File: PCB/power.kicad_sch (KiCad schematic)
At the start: 7 parts, among them U4 TPS628438DRL, U5 TPS3839K33

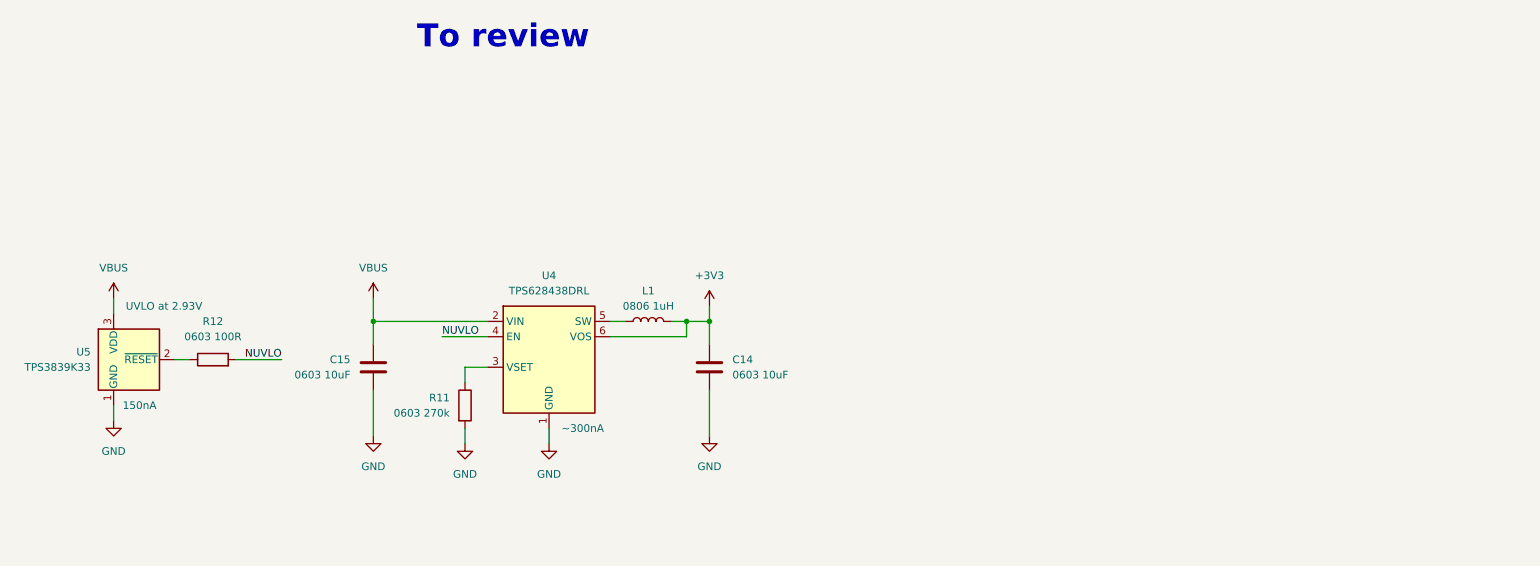
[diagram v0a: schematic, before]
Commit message: added power block, pheripherial
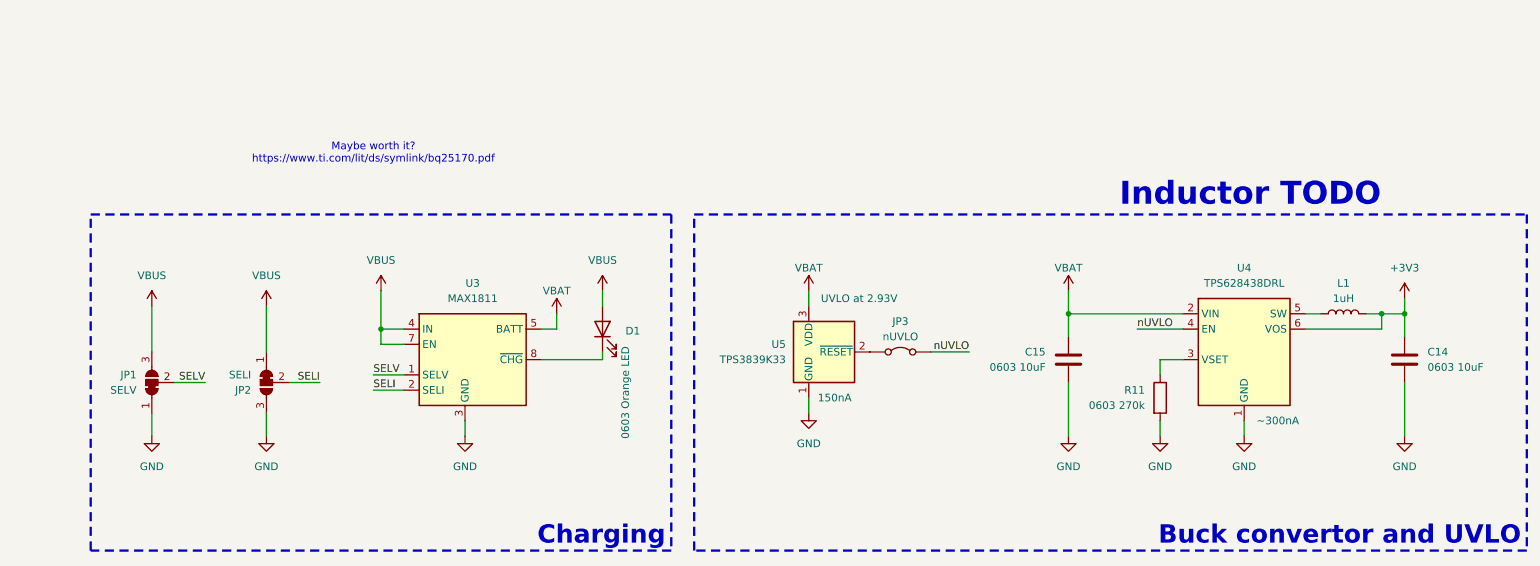
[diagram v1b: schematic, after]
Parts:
- removed R12: 0603 100R, symbol Device:R
- added D1: 0603 Orange LED, LED_SMD:LED_0603_1608Metric_Pad1.05x0.95mm_HandSolder, symbol Device:LED
- added JP1: SELV, symbol Jumper:SolderJumper_3_Bridged12
- added JP2: SELI, symbol Jumper:SolderJumper_3_Bridged12
- added JP3: nUVLO, symbol Jumper:Jumper_2_Bridged
- added U3: MAX1811, Package_SO:SOIC-8_3.9x4.9mm_P1.27mm, symbol Battery_Management:MAX1811
- L1: value 0806 1uH -> 1uH
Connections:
- net GND: now also JP1.1 (A), JP2.3 (B), U3.3 (GND), U3.6 (GND)
- net VBUS: now also D1.2 (A), JP1.3 (B), JP2.1 (A), U3.4 (IN), U3.7 (EN); no longer C15.1, U4.2 (VIN), U5.3 (VDD)
- net at U5.2 (~{RESET}): now also JP3.1 (A)
- net NUVLO renamed nUVLO
- net nUVLO: now also JP3.2 (B)
- new net: D1.1 (K), U3.8 (~{CHG})
- new net SELI: JP2.2 (C), U3.2 (SELI)
- new net SELV: JP1.2 (C), U3.1 (SELV)
- new net VBAT: C15.1, U3.5 (BATT), U4.2 (VIN), U5.3 (VDD)
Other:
- note added: "Inductor TODO"
- note added: "Maybe worth it? https://www.ti.com/lit/ds/symlink/bq25170.pdf"
- note removed: "To review"
- moved on the sheet: C14, C15, L1, R11, U4, U5

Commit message: added GPS, charging IC, SHT41, and started working on the RF
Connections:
- net GND renamed GNDREF
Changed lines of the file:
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@@
 	)
 	(symbol
-		(lib_id "power:GND")
+		(lib_id "power:GNDREF")
 		(at 190.5 113.03 0)
 		(unit 1)
@@
 		(dnp no)
 		(fields_autoplaced yes)
-		(property "Reference" "#PWR040"
+		(property "Reference" "#PWR40"
 			(at 190.5 119.38 0)
 			(hide yes)
@@
 			)
 		)
-		(property "Value" "GND"
+		(property "Value" "GNDREF"
 			(at 190.5 118.11 0)
 			(show_name no)
@@
 			)
 		)
-		(property "Description" "Power symbol creates a global label with name \"GND\" , ground"
+		(property "Description" "Power symbol creates a global label with name \"GNDREF\" , reference supply ground"
 			(at 190.5 113.03 0)
 			(hide yes)
@@
 			(project "PawBuddy_PCB"
 				(path "/ddc031a5-f801-471f-9629-7d18bb02ea71/bbb75299-8683-40e9-bcaa-d3bebe81f345"
-					(reference "#PWR040")
-					(unit 1)
-				)
-			)
-		)
-	)
-	(symbol
-		(lib_id "power:GND")
+					(reference "#PWR40")
+					(unit 1)
+				)
+			)
+		)
+	)
+	(symbol
+		(lib_id "power:GNDREF")
 		(at 246.38 113.03 0)
 		(unit 1)
@@
 		(dnp no)
 		(fields_autoplaced yes)
-		(property "Reference" "#PWR041"
+		(property "Reference" "#PWR41"
 			(at 246.38 119.38 0)
 			(hide yes)
@@
 			)
 		)
-		(property "Value" "GND"
+		(property "Value" "GNDREF"
 			(at 246.38 118.11 0)
 			(show_name no)
@@
 			)
 		)
-		(property "Description" "Power symbol creates a global label with name \"GND\" , ground"
+		(property "Description" "Power symbol creates a global label with name \"GNDREF\" , reference supply ground"
 			(at 246.38 113.03 0)
 			(hide yes)
@@
 			(project "PawBuddy_PCB"
 				(path "/ddc031a5-f801-471f-9629-7d18bb02ea71/bbb75299-8683-40e9-bcaa-d3bebe81f345"
-					(reference "#PWR041")
+					(reference "#PWR41")
 					(unit 1)
 				)
@@
 	)
 	(symbol
-		(lib_id "power:GND")
+		(lib_id "power:GNDREF")
 		(at 57.15 113.03 0)
 		(unit 1)
@@
 		(dnp no)
 		(fields_autoplaced yes)
-		(property "Reference" "#PWR049"
+		(property "Reference" "#PWR49"
 			(at 57.15 119.38 0)
 			(hide yes)
@@
 			)
 		)
-		(property "Value" "GND"
+		(property "Value" "GNDREF"
 			(at 57.15 118.11 0)
 			(show_name no)
@@
 			)
 		)
-		(property "Description" "Power symbol creates a global label with name \"GND\" , ground"
+		(property "Description" "Power symbol creates a global label with name \"GNDREF\" , reference supply ground"
 			(at 57.15 113.03 0)
 			(hide yes)
@@
 			(project "PawBuddy_PCB"
 				(path "/ddc031a5-f801-471f-9629-7d18bb02ea71/bbb75299-8683-40e9-bcaa-d3bebe81f345"
-					(reference "#PWR049")
-					(unit 1)
-				)
-			)
-		)
-	)
-	(symbol
-		(lib_id "power:GND")
+					(reference "#PWR49")
+					(unit 1)
+				)
+			)
+		)
+	)
+	(symbol
+		(lib_id "power:GNDREF")
 		(at 147.32 109.22 0)
 		(unit 1)
@@
 		(dnp no)
 		(fields_autoplaced yes)
-		(property "Reference" "#PWR038"
+		(property "Reference" "#PWR38"
 			(at 147.32 115.57 0)
 			(hide yes)
@@
 			)
 		)
-		(property "Value" "GND"
+		(property "Value" "GNDREF"
 			(at 147.32 114.3 0)
 			(show_name no)
@@
 			)
 		)
-		(property "Description" "Power symbol creates a global label with name \"GND\" , ground"
+		(property "Description" "Power symbol creates a global label with name \"GNDREF\" , reference supply ground"
 			(at 147.32 109.22 0)
 			(hide yes)
@@
 			(project "PawBuddy_PCB"
 				(path "/ddc031a5-f801-471f-9629-7d18bb02ea71/bbb75299-8683-40e9-bcaa-d3bebe81f345"
-					(reference "#PWR038")
+					(reference "#PWR38")
 					(unit 1)
 				)
@@
 	)
 	(symbol
-		(lib_id "power:GND")
+		(lib_id "power:GNDREF")
 		(at 90.17 113.03 0)
 		(unit 1)
@@
 		(dnp no)
 		(fields_autoplaced yes)
-		(property "Reference" "#PWR046"
+		(property "Reference" "#PWR46"
 			(at 90.17 119.38 0)
 			(hide yes)
@@
 			)
 		)
-		(property "Value" "GND"
+		(property "Value" "GNDREF"
 			(at 90.17 118.11 0)
 			(show_name no)
@@
 			)
 		)
-		(property "Description" "Power symbol creates a global label with name \"GND\" , ground"
+		(property "Description" "Power symbol creates a global label with name \"GNDREF\" , reference supply ground"
 			(at 90.17 113.03 0)
 			(hide yes)
@@
 			(project "PawBuddy_PCB"
 				(path "/ddc031a5-f801-471f-9629-7d18bb02ea71/bbb75299-8683-40e9-bcaa-d3bebe81f345"
-					(reference "#PWR046")
+					(reference "#PWR46")
 					(unit 1)
 				)
@@
 	)
 	(symbol
-		(lib_id "power:GND")
+		(lib_id "power:GNDREF")
 		(at 38.1 113.03 0)
 		(unit 1)
@@
 		(dnp no)
 		(fields_autoplaced yes)
-		(property "Reference" "#PWR045"
+		(property "Reference" "#PWR45"
 			(at 38.1 119.38 0)
 			(hide yes)
@@
 			)
 		)
-		(property "Value" "GND"
+		(property "Value" "GNDREF"
 			(at 38.1 118.11 0)
 			(show_name no)
@@
 			)
 		)
-		(property "Description" "Power symbol creates a global label with name \"GND\" , ground"
+		(property "Description" "Power symbol creates a global label with name \"GNDREF\" , reference supply ground"
 			(at 38.1 113.03 0)
 			(hide yes)
@@
 			(project "PawBuddy_PCB"
 				(path "/ddc031a5-f801-471f-9629-7d18bb02ea71/bbb75299-8683-40e9-bcaa-d3bebe81f345"
-					(reference "#PWR045")
-					(unit 1)
-				)
-			)
-		)
-	)
-	(symbol
-		(lib_id "power:GND")
+					(reference "#PWR45")
+					(unit 1)
+				)
+			)
+		)
+	)
+	(symbol
+		(lib_id "power:GNDREF")
 		(at 219.71 113.03 0)
 		(unit 1)
@@
 		(dnp no)
 		(fields_autoplaced yes)
-		(property "Reference" "#PWR037"
+		(property "Reference" "#PWR37"
 			(at 219.71 119.38 0)
 			(hide yes)
@@
 			)
 		)
-		(property "Value" "GND"
+		(property "Value" "GNDREF"
 			(at 219.71 118.11 0)
 			(show_name no)
@@
 			)
 		)
-		(property "Description" "Power symbol creates a global label with name \"GND\" , ground"
+		(property "Description" "Power symbol creates a global label with name \"GNDREF\" , reference supply ground"
 			(at 219.71 113.03 0)
 			(hide yes)
@@
 			(project "PawBuddy_PCB"
 				(path "/ddc031a5-f801-471f-9629-7d18bb02ea71/bbb75299-8683-40e9-bcaa-d3bebe81f345"
-					(reference "#PWR037")
+					(reference "#PWR37")
 					(unit 1)
 				)
@@
 	)
 	(symbol
-		(lib_id "power:GND")
+		(lib_id "power:GNDREF")
 		(at 205.74 113.03 0)
 		(unit 1)
@@
 		(dnp no)
 		(fields_autoplaced yes)
-		(property "Reference" "#PWR039"
+		(property "Reference" "#PWR39"
 			(at 205.74 119.38 0)
 			(hide yes)
@@
 			)
 		)
-		(property "Value" "GND"
+		(property "Value" "GNDREF"
 			(at 205.74 118.11 0)
 			(show_name no)
@@
 			)
 		)
-		(property "Description" "Power symbol creates a global label with name \"GND\" , ground"
+		(property "Description" "Power symbol creates a global label with name \"GNDREF\" , reference supply ground"
 			(at 205.74 113.03 0)
 			(hide yes)
@@
 			(project "PawBuddy_PCB"
 				(path "/ddc031a5-f801-471f-9629-7d18bb02ea71/bbb75299-8683-40e9-bcaa-d3bebe81f345"
-					(reference "#PWR039")
-					(unit 1)
-				)
+					(reference "#PWR39")
+					(unit 1)
+				)

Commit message: a bit of polishing and work on the pheripherials
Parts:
- added J1: SM02B-SRSS-TB, Connector_JST:JST_SH_SM02B-SRSS-TB_1x02-1MP_P1.00mm_Horizontal, symbol Connector_Generic_MountingPin:Conn_01x02_MountingPin
- C14: value 0603 10uF -> 10uF
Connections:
- net GNDREF: now also J1.2 (Pin_2), J1.MP (MountPin)
- net VBAT: now also J1.1 (Pin_1)
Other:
- note added: "Leave out in the production version"
- moved on the sheet: C14, D1, JP1, JP2, U3
